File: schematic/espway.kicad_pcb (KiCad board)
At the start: 2 copper layers, 43 x 34.2 mm, 37 parts, among them J1 CONN_01X02, J2 CONN_01X02, J3 Conn_01x05_Male, SW1 SW_Push, U1 LM1117-3.3, U2 ESP-12E, U3 DRV8835, U4 LSM6DS3

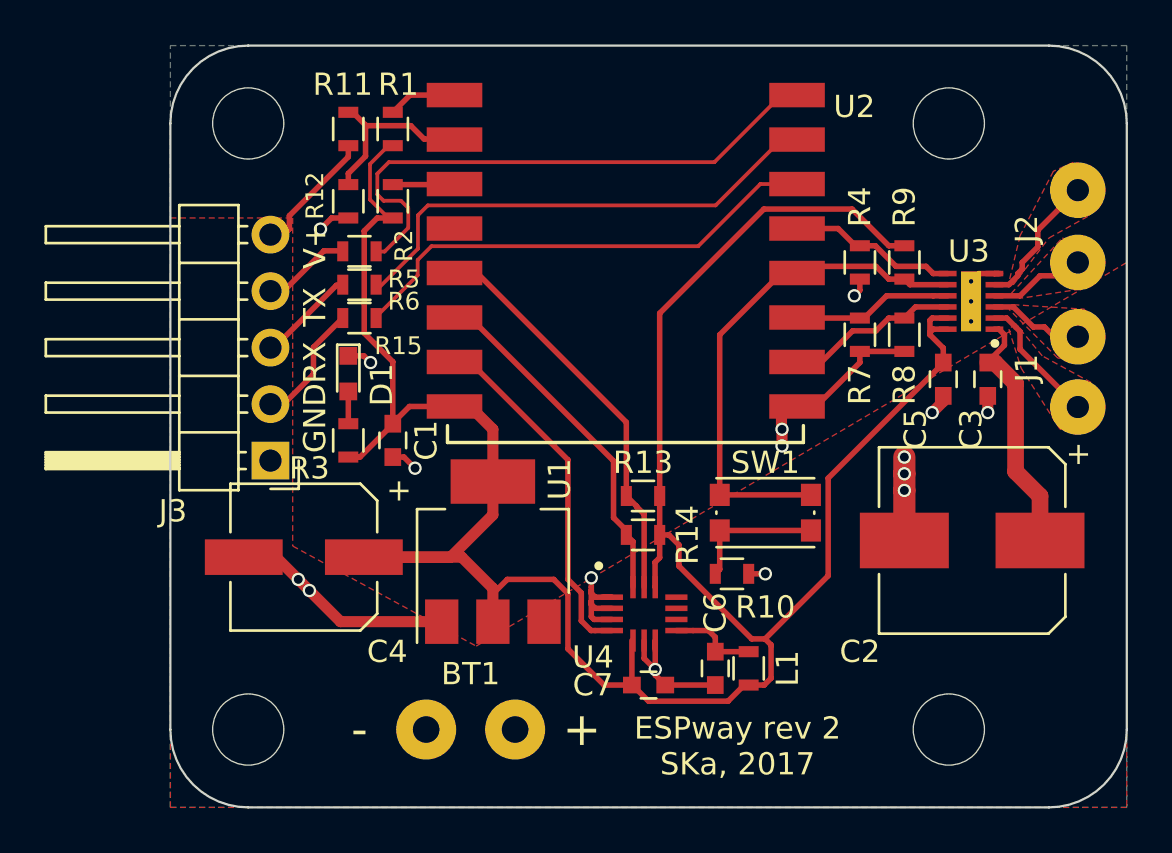
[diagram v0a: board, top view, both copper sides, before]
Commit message: schematic & pcb: pullup fixes etc
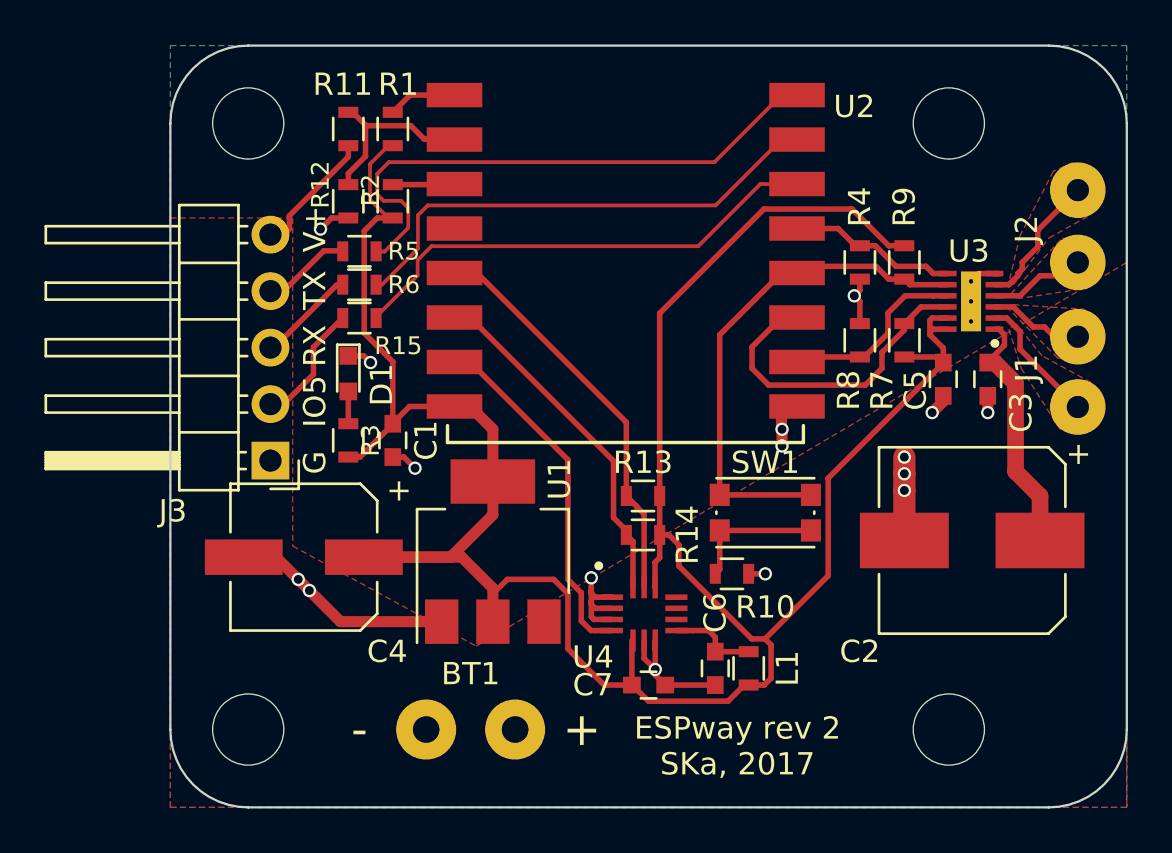
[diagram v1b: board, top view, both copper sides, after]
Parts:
- R10, R15, R5, R6: value 100 -> 330
- moved R7 2.02 mm to (160.0, 134.0), turned to 90 degrees
- moved R8 2.02 mm to (158.0, 134.0), turned to 90 degrees
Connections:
- R7 pad 1: AENBL -> +3V3
- R7 pad 2: GND -> APHASE
- R8 pad 1: APHASE -> AENBL
- U2 pad 10: APHASE -> AENBL
- U2 pad 11: AENBL -> APHASE
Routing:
- net APHASE: track 8.50 -> 14.0 mm
- net GND: track 45.1 -> 41.0 mm
- net AENBL: track 7.90 -> 11.0 mm
- net +3V3: track 116.6 -> 118.4 mm
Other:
- board text added: "G"
- board text added: "IO5"
- board text removed: "GND"

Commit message: Minor PCB track adjustments
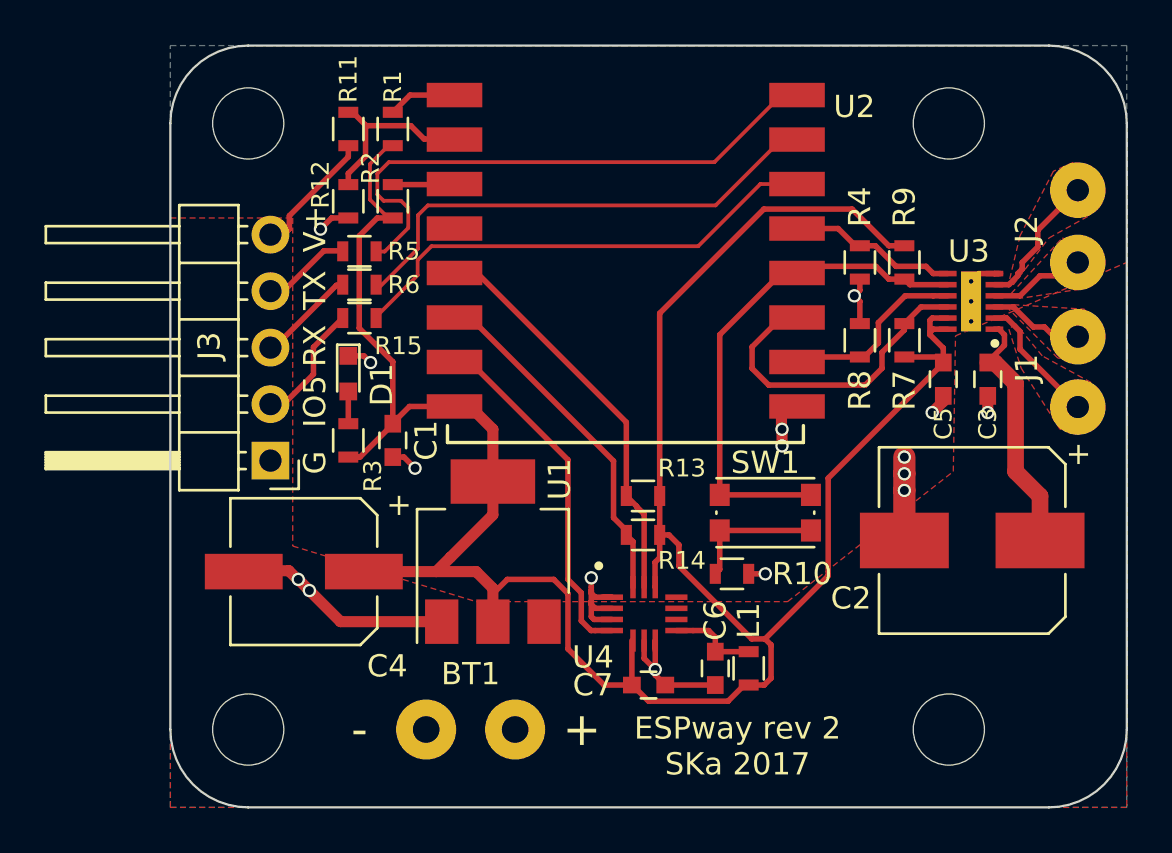
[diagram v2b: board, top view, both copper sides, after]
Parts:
- moved C4 0.65 mm to (133.0, 144.4)
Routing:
- net +3V3: track 118.4 -> 115.4 mm
- net GND: track 41.0 -> 39.7 mm
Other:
- board text added: "ESPway rev 2 SKa 2017"
- board text removed: "ESPway rev 2 SKa, 2017"
